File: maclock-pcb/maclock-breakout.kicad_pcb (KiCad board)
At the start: 2 copper layers, 70.5 x 26.5 mm, 19 parts, among them J1 BM02B-SRSS-TB(LF)(SN), J2 BM04B-SRSS-TB(LF)(SN), J3 B2B-PH-SM4-TB(LF)(SN), SW1 TSB001A3518A, SW2 TSB001A3518A, U1 PAM8302AASCR

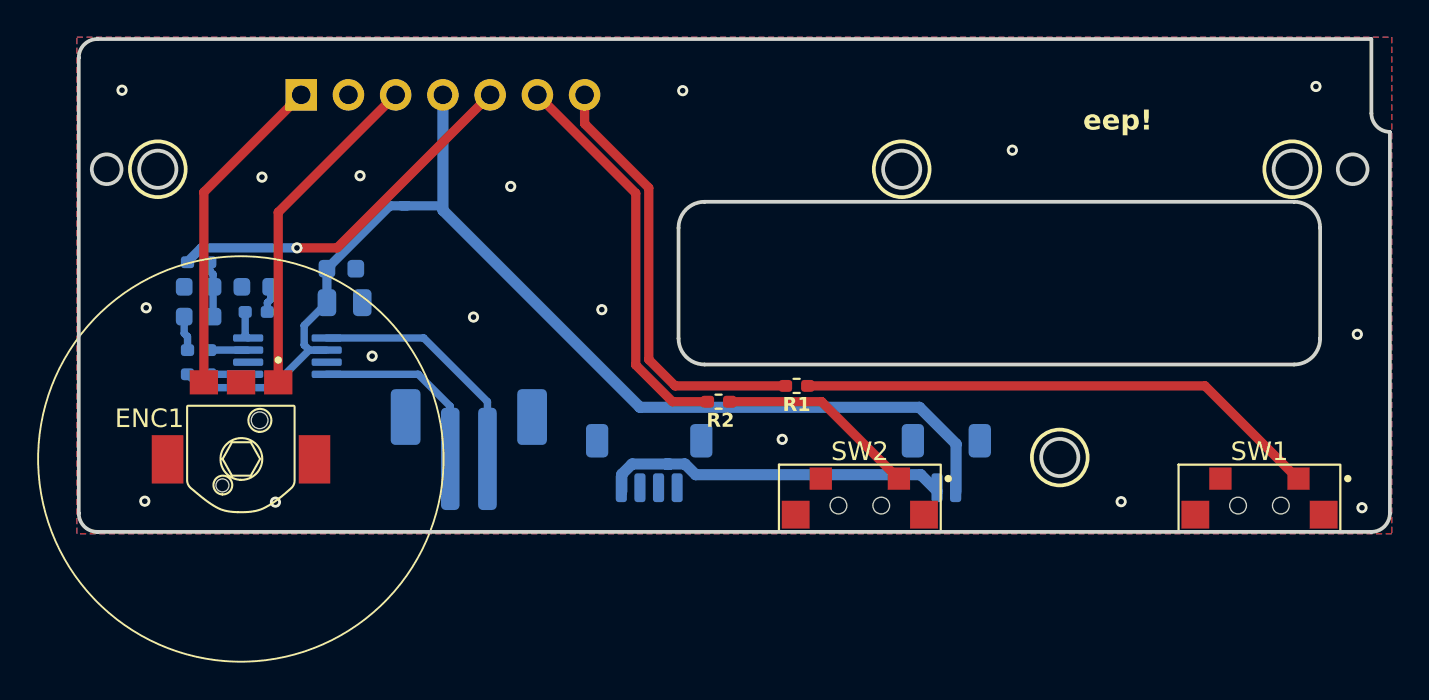
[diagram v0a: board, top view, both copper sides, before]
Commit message: PCB rev 2026.10: E8E8 dial, LCSC switches, PicoBlade connectors, clean schematic
Connectors: J1, J2 and J3 are Molex PicoBlade 1.25 mm (53398-0271 /
53398-0471), the pitch of the Maclock's own power, switch and speaker plugs;
the JST SH/PH parts on the first boards did not take them. The three now share
one row, 0.6 mm closer to the bottom edge, which also moves ENC1's rear post
hole out of J3's courtyard.

ENC1 is the F-Switch E8E8-3.2C60-9B34 (1.74 mm hex bore; the HYCW03's 1.78 mm
was too loose for the dial), sold by dicomon and not stocked at LCSC. Its
footprint is the proto board's Dial land with the origin on the bore, its
outline and 3D model (build123d STEP) are measured from a real part, and the
silkscreen shows the body and the 21 mm wheel's clearance. The symbol is KiCad's
encoder with an MP pin for the solder tabs. ENC_A/ENC_B are routed on F.Cu
straight to the pad centres.

SW1/SW2 use LCSC's own TSB001A3518A symbol, footprint and STEP (C2888448), in a
new `lcsc` project library imported with easyeda2kicad. Only the conversion
artefacts are fixed: NPTH peg holes, no outline stroke on the bracket pads (it
made them fail edge clearance), passive pins, one closed courtyard. The one-off
switch footprint and the HYCW03 footprint are gone; `maclock` now holds ENC1
only.

The schematic is rebuilt as one A4 sheet in functional blocks (Raspberry Pi,
power, buttons, dial, audio amplifier) with power symbols, notes and a filled
title block. Every part carries Manufacturer, MPN and LCSC fields, and ENC1 a
dicomon Supplier and link, so any exported BOM names the source. PiInput is J4.
Board nets and fields follow (GND, +5V, no-connect nets): schematic parity 0.

Also: C4/C5 ground pads get thermal reliefs (C1/C3 sit in pour too broken up to
form spokes and stay solid); the OSHW logo is removed, since the CC BY-NC-SA
licence is outside the OSHW definition; the board has a title block.
production/ (kicad-cli fab outputs) and the Fabrication Toolkit's options file
are 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
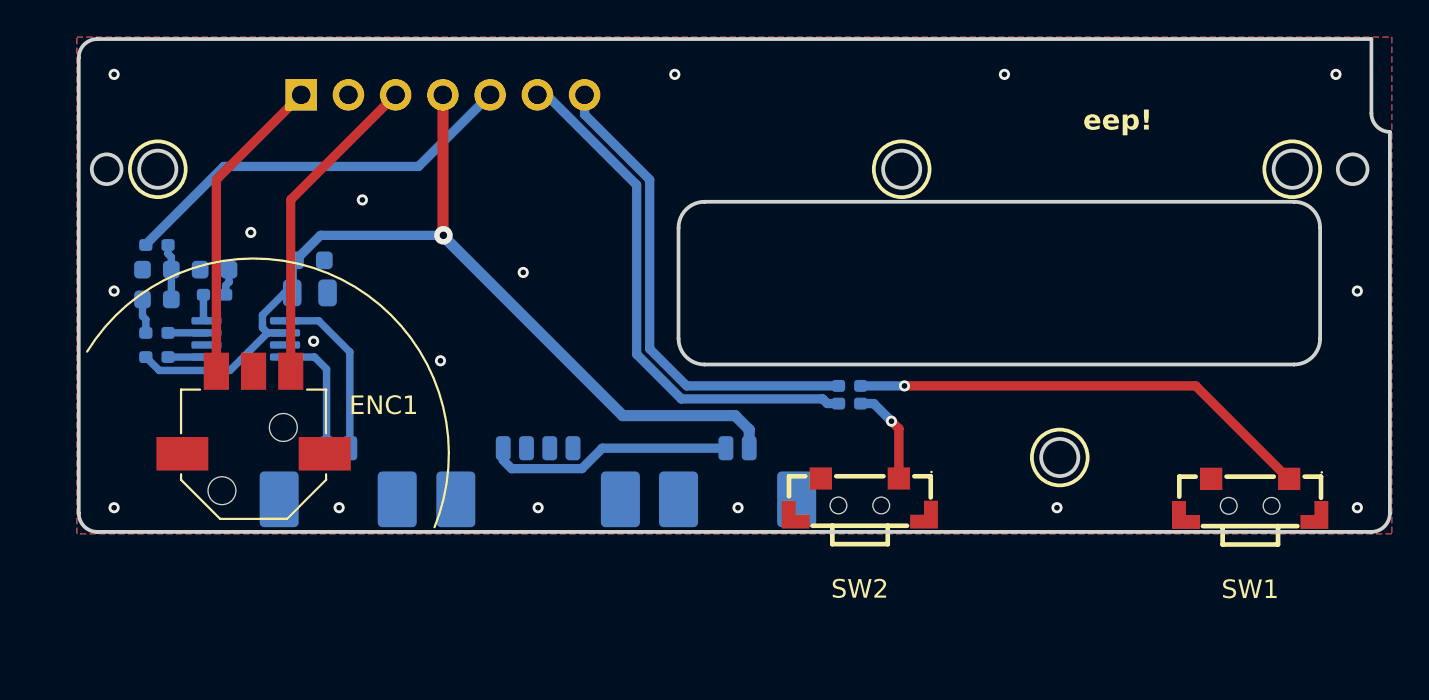
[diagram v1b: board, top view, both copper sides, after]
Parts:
- ENC1: value HYCW03-2.8D-5P-S -> E8E8-3.2C60-9B34; footprint maclock:RotaryEncoder_HYCW03-2.8D-5P-S_SMD -> maclock:RotaryEncoder_E8E8-3.2C60-9B34_SMD
- J1: value BM02B-SRSS-TB(LF)(SN) -> 53398-0271; footprint Connector_JST:JST_SH_BM02B-SRSS-TB_1x02-1MP_P1.00mm_Vertical -> Connector_Molex:Molex_PicoBlade_53398-0271_1x02-1MP_P1.25mm_Vertical
- J2: value BM04B-SRSS-TB(LF)(SN) -> 53398-0471; footprint Connector_JST:JST_SH_BM04B-SRSS-TB_1x04-1MP_P1.00mm_Vertical -> Connector_Molex:Molex_PicoBlade_53398-0471_1x04-1MP_P1.25mm_Vertical
- J3: value B2B-PH-SM4-TB(LF)(SN) -> 53398-0271; footprint Connector_JST:JST_PH_B2B-PH-SM4-TB_1x02-1MP_P2.00mm_Vertical -> Connector_Molex:Molex_PicoBlade_53398-0271_1x02-1MP_P1.25mm_Vertical
- J4: renamed from PiInput; value PZ254V-11-07P -> Pi GPIO
- R1, R2: value 1K -> 1k; moved to B.Cu
- R3: value 1K -> 1k
- R4, R5: value 47K -> 47k
- R6: value 100K -> 100k
- SW1, SW2: footprint maclock:SW_TSB001_7.7x3.55_SideSMD -> lcsc:SW-SMD_TSB001XXXX
- moved J1 11.2 mm to (152.9, 101.2)
- moved J3 7.12 mm to (131.4, 101.2)
- moved R2 7.05 mm to (158.9, 97.6)
- moved J2 5.99 mm to (142.2, 101.2)
- moved R1 2.85 mm to (158.9, 96.7)
- moved C3 2.43 mm to (124.8, 90.4)
- moved R5 2.43 mm to (124.8, 91.8)
- moved R6 2.43 mm to (121.7, 95.1)
- moved C1 2.43 mm to (121.7, 90.4)
- moved C2 2.43 mm to (121.7, 92.0)
- moved R3 2.43 mm to (121.7, 89.1)
- moved R4 2.43 mm to (121.7, 93.8)
- moved U1 2.43 mm to (126.5, 94.1)
- moved C5 1.94 mm to (129.9, 91.7)
- moved ENC1 1.89 mm to (126.9, 100.3), turned to 0 degrees
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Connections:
- net /5V renamed +5V
- C1 pad 1: /GND -> GND
- C3 pad 1: /GND -> GND
- C4 pad 2: /GND -> GND
- C5 pad 2: /GND -> GND
- ENC1 pad C: /GND -> GND
- J2 pad 1: (no net) -> unconnected-(J2-Pin_1-Pad1)
- J2 pad 2: (no net) -> unconnected-(J2-Pin_2-Pad2)
- J2 pad 3: /GND -> GND
- J4 pad 2: /GND -> GND
- SW1 pad 2: /GND -> GND
- SW1 pad 3: /GND -> GND
- SW1 pad 4: /GND -> GND
- SW2 pad 2: /GND -> GND
- SW2 pad 3: /GND -> GND
- SW2 pad 4: /GND -> GND
- U1 pad 2: (no net) -> unconnected-(U1-NC-Pad2)
- U1 pad 7: /GND -> GND
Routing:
- net +5V: track 63.1 -> 51.7 mm, vias 0 -> 1
- net /BTN2: track 21.4 -> 28.4 mm
- net /5V_IN: track 18.8 -> 13.3 mm
- net /SW2: track 10.8 -> 5.44 mm, vias 0 -> 1
- net /SPK+: track 13.1 -> 9.35 mm
- net /SPK-: track 10.2 -> 6.76 mm
- net /SW1: track 28.3 -> 25.2 mm, vias 0 -> 1
- net /BTN1: track 23.6 -> 26.1 mm
- net /AUDIO: track 20.0 -> 21.9 mm, vias 1 -> 0
- net /ENC_B: track 17.6 -> 16.7 mm
- net /ENC_A: track 18.1 -> 17.2 mm
- net GND: vias 0 -> 17
- net /GND: vias 17 -> 0
- added copper zone on B.Cu, net GND
- added copper zone on F.Cu, net GND
- removed copper zone on B.Cu, net /GND
- removed copper zone on F.Cu, net /GND
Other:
- board text added: "Wells Workshop https://wells.ee"
- board text added: "rev 2026.10"
- board text removed: "+"
- board text removed: "-"
- board text removed: "by Wells Workshop - https://wells.ee"
- board text removed: "rev 2026.09"

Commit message: Breakout: put back the Switch / Power / Speaker labels and J2's + / -
Rev 2026.10's field cleanup deleted the board-only "Label" field that
named J1-J3 on the back silk, leaving three identical PicoBlade sockets
and no polarity mark on the power input. The labels are back above the
connectors, now as a "Label" field on the schematic symbols too, so an
Update PCB from Schematic can't strip them again. "Speaker" sits 0.3 mm
right of centre to clear ENC1's peg hole. J2 gets + over pin 4 (5V) and
- over pin 3 (GND), as before.
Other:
- board text added: "+"
- board text added: "-"
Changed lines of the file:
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@@
 			)
 		)
+		(property "Label" "Speaker"
+			(at -0.3 4.2 0)
+			(layer "B.SilkS")
+			(effects
+				(font
+					(size 1.0795 1.0795)
+					(thickness 0.1905)
+				)
+				(justify mirror)
+			)
+		)
 		(attr smd)
 		(duplicate_pad_numbers_are_jumpers no)
@@
 			)
 		)
+		(property "Label" "Switch"
+			(at 0 4.2 0)
+			(layer "B.SilkS")
+			(effects
+				(font
+					(size 1.0795 1.0795)
+					(thickness 0.1905)
+				)
+				(justify mirror)
+			)
+		)
 		(attr smd)
 		(duplicate_pad_numbers_are_jumpers no)
@@
 			)
 		)
+		(property "Label" "Power"
+			(at 0 4.2 0)
+			(layer "B.SilkS")
+			(effects
+				(font
+					(size 1.0795 1.0795)
+					(thickness 0.1905)
+				)
+				(justify mirror)
+			)
+		)
 		(attr smd)
 		(duplicate_pad_numbers_are_jumpers no)
@@
 		)
 	)
+	(gr_text "+"
+		(at 140.325 98.5 0)
+		(layer "B.SilkS")
+		(effects
+			(font
+				(size 0.8 0.8)
+				(thickness 0.15)
+			)
+			(justify mirror)
+		)
+	)
+	(gr_text "-"
+		(at 141.575 98.5 0)
+		(layer "B.SilkS")
+		(effects
+			(font
+				(size 0.8 0.8)
+				(thickness 0.15)
+			)
+			(justify mirror)
+		)
+	)

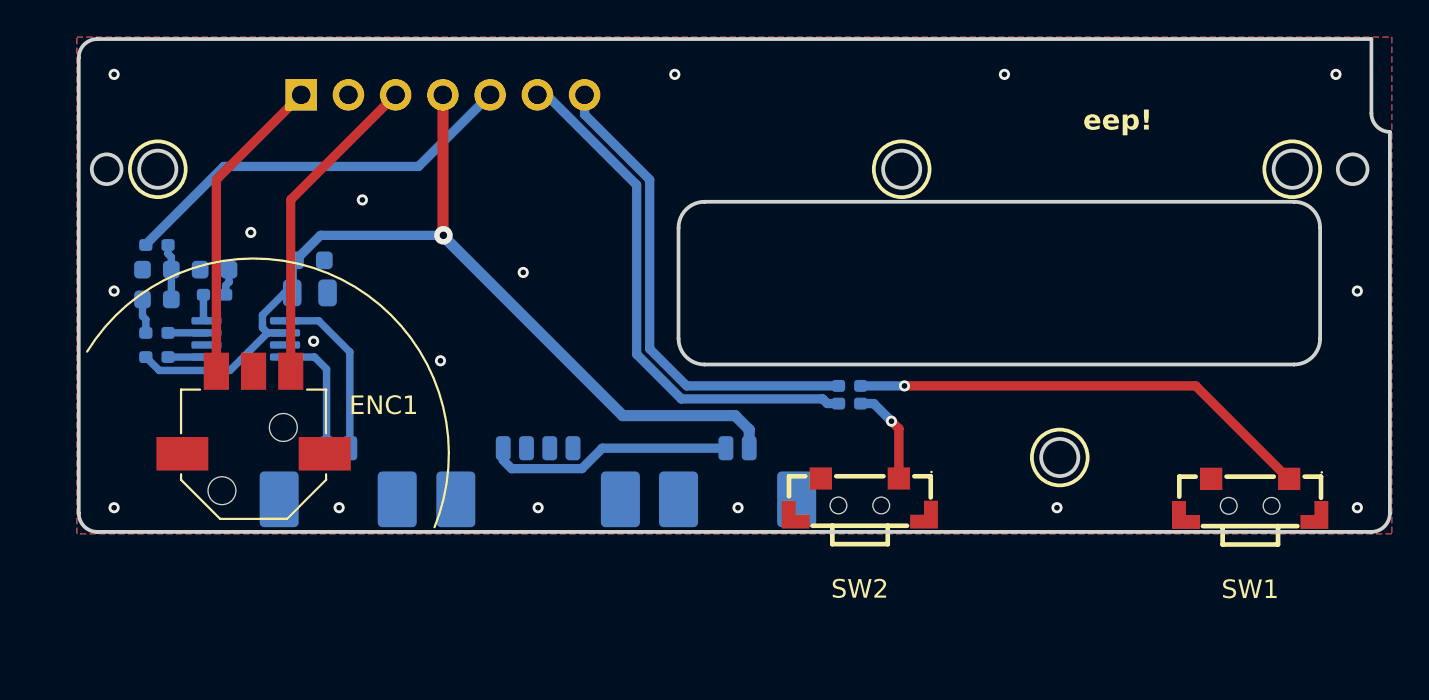
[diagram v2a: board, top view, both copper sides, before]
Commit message: PCB rev 2026.11: buffered audio input and a separate Pi ground return
Rev 2026.10 whines faintly with the Pi running. Recorded on the board and
traced, with the Pi powered both ways:

- The Pi's own supply current (Pi, display, backlight) ran through the
  amp's ground. Moving the Pi to USB power dropped the backlight's 1 kHz
  comb about 28 dB and removed the emulator's drifting tones. Holding
  GPIO 19 low or floating changed nothing on board power.
- On USB power, what was left rode on the audio pin itself: a 60 Hz-pulsed
  buzz from the Pi's 3.3 V (only while GPIO 19 runs PWM), and hiss from the
  Pi-to-board ground offset (gone when the pin floats).

Four new parts:

- J4 pin 2 is its own net, GND_PI, routed straight to J2 and joined to the
  board ground by net tie NT1 (copper only) at J2's ground pin. The amp's
  ground no longer carries the Pi's current.
- U2 (SN74LVC1G17) rebuilds GPIO 19 from U3 (TPS7A2033, low-noise 3.3 V),
  so only the timing of the Pi's signal reaches R3/C1 and the amp. C8 is
  U3's input cap; C10 sits between U3 and U2 as U3's output cap and U2's
  bypass. Both are the 1 uF part C4 already uses. R6 pulls SD up to the
  3.3 V rail, right beside U2.

Layout:

- U2, R3/C1 and R6 sit just left of U1, with U3, C8 and C10 tucked in
  beside U2, clear of the board edge.
- The amp and U3 take their 5 V from J1, at the start of the 5 V trunk, so
  the Pi's current on the trunk shares no copper with the amp's supply.
  That branch stays on the bottom layer and crosses under U1 between its
  pin rows rather than under the speaker leads, which leaves the top-layer
  ground plane unbroken under the amp. C4 stays against U1's VDD/GND
  pins; U1 turned so its outputs face J3.
- The audio line runs over the top of J4 on the bottom layer, so it never
  crosses GND_PI: no vias, header pinout unchanged.
- J1 (switch) and J2 (power) trade places, so NT1 and the 5 V tap sit at
  the ends of short, straight runs. Their silk labels move with them; J2's
  "+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
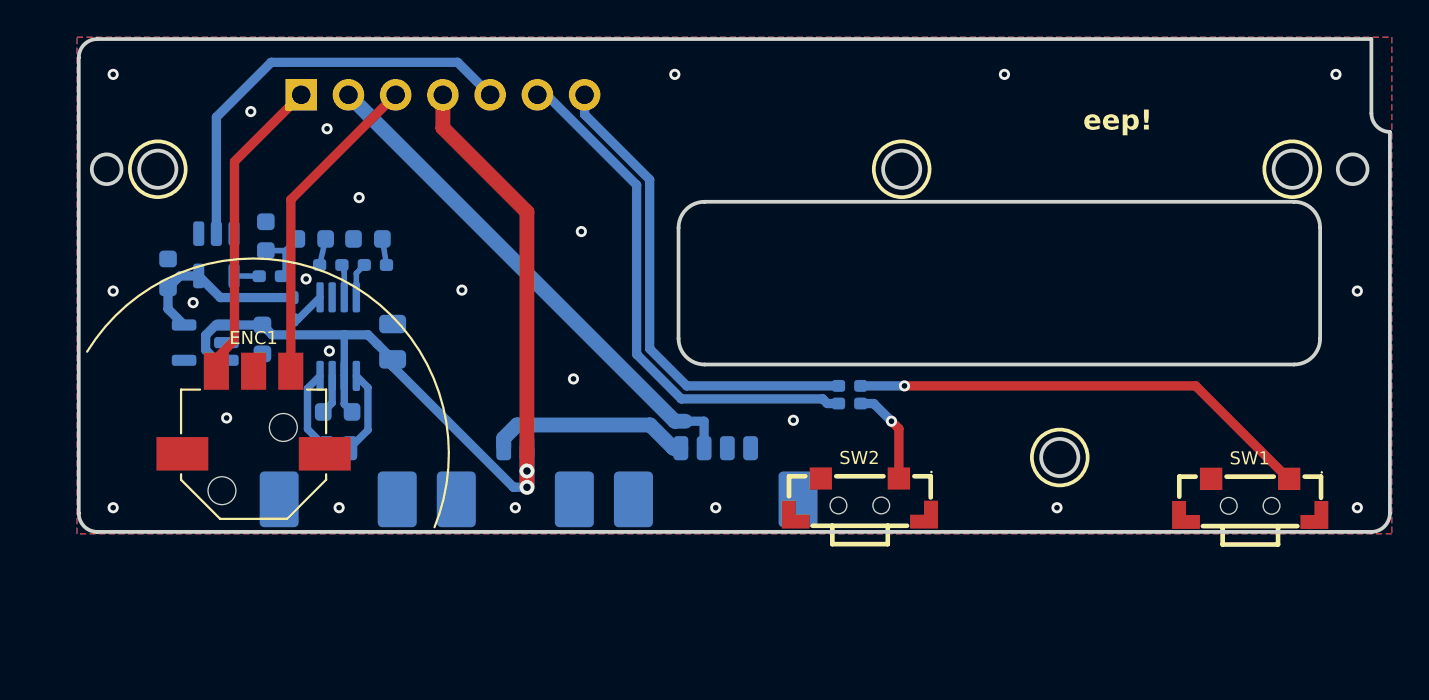
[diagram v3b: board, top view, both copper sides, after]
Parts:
- added C10: 1uF, Capacitor_SMD:C_0603_1608Metric, B.Cu at (122.3, 90.6)
- added C8: 1uF, Capacitor_SMD:C_0603_1608Metric, B.Cu at (127.4, 94.2)
- added NT1: NetTie_2, NetTie:NetTie-2_SMD_Pad0.5mm, B.Cu at (150.6, 98.5)
- added U2: SN74LVC1G17DBVR, Package_TO_SOT_SMD:SOT-23-5, B.Cu at (124.9, 89.6)
- added U3: TPS7A2033PDBVR, Package_TO_SOT_SMD:SOT-23-5, B.Cu at (124.3, 94.3)
- moved J1 12.0 mm to (141.0, 101.2)
- moved R4 10.0 mm to (131.1, 90.2)
- moved J2 9.55 mm to (151.8, 101.2)
- moved C2 8.91 mm to (130.0, 88.8), turned to 0 degrees
- moved R5 8.79 mm to (133.4, 90.2)
- moved C3 8.41 mm to (133.1, 88.8)
- moved C4 8.29 mm to (131.4, 98.0), turned to 180 degrees
- moved R6 7.75 mm to (129.0, 92.5), turned to -90 degrees
- moved R3 6.32 mm to (127.8, 90.8)
- moved C1 6.13 mm to (127.6, 88.6), turned to 90 degrees
- moved C5 5.16 mm to (134.4, 94.3), turned to 90 degrees
- moved U1 4.97 mm to (131.4, 94.0), turned to -90 degrees
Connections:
- C1 pad 1: GND -> /A+
- C1 pad 2: /A+ -> GND
- J4 pad 2: GND -> /GND_PI
- R3 pad 1: /AUDIO -> Net-(R3-Pad1)
- R6 pad 1: +5V -> +3V3
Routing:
- net /GND_PI: track 0.00 -> 25.4 mm
- net +3V3: track 0.00 -> 9.80 mm
- net /SPK+: track 9.35 -> 4.55 mm
- net GND: track 0.00 -> 3.59 mm, vias 17 -> 23
- net /5V_IN: track 13.3 -> 10.9 mm
- net /SPK-: track 6.76 -> 4.59 mm
- net Net-(R3-Pad1): track 0.00 -> 1.35 mm
- net +5V: track 51.7 -> 52.9 mm, vias 1 -> 2
- net /AUDIO: track 21.9 -> 22.9 mm
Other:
- board text added: "rev 2026.11"
- board text removed: "rev 2026.10"

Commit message: Battery supply is about 4 V: document the burble, drop U3 to 3.0 V
The Maclock's charging board doesn't boost the 18650 to 5 V. Its output is
the cell: about 4.15 V with no load and 4.00 V with the Pi running, and the
same with the charge cable plugged in. vcgencmd get_throttled still read 0x0
at 4.00 V, so the Pi doesn't catch it.

On a rev 2026.10 board this puts a constant burble in the speaker, louder
as the brightness goes up. A phone recording with GPIO 19 switched from PWM
to a static low (emulator still running) shows the 3-4.25 kHz and
5.5-6 kHz noise falling about 10 dB to the floor and returning with PWM. So
it rides on the audio pin's high level, the Pi's 3.3 V made from ~4 V, and
the amp's own supply and ground are clean. That is the path rev 2026.11's
U2/U3 rebuild takes out.

U3 TPS7A2033 -> TPS7A2030 (LCSC C963429, same SOT-23-5, no layout change),
net +3V3 renamed +3V0. A 3.3 V LDO has about 0.7 V of headroom at full
charge and runs into dropout as the cell drains, where it stops filtering;
3.0 V keeps it regulating over the battery's range. The audio drive drops
0.8 dB, which offsets some of the amp's lost headroom at 4 V. TPS7A20 takes
1.6-6.0 V in, so a real 5 V supply is fine too. ERC 0; DRC unchanged (0
unconnected, 0 parity); netlist identical apart from the rename.

Docs: a Known Issues entry and a troubleshooting line for the burble, and
every claim that the board or Pi runs on 5 V now says about 4 V. Pin and
net names (5V, +5V) stay as labels. The interposer drawing's aria-label
still says "5 V"; it's exported from the shop, so that fix belongs there.
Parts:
- U3: value TPS7A2033PDBVR -> TPS7A2030PDBVR
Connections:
- net +3V3 renamed +3V0
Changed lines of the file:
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@@
 			(layers "B.Cu" "B.Mask" "B.Paste")
 			(roundrect_rratio 0.25)
-			(net "+3V3")
+			(net "+3V0")
 		)
 		(embedded_fonts no)
@@
 			(layers "B.Cu" "B.Mask" "B.Paste")
 			(roundrect_rratio 0.25)
-			(net "+3V3")
+			(net "+3V0")
 		)
 		(pad "2" smd roundrect
@@
 			(layers "B.Cu" "B.Mask" "B.Paste")
 			(roundrect_rratio 0.25)
-			(net "+3V3")
+			(net "+3V0")
 		)
 		(pad "2" smd roundrect
@@
 			)
 		)
-		(property "Value" "TPS7A2033PDBVR"
+		(property "Value" "TPS7A2030PDBVR"
 			(at 0 -2.4 0)
 			(layer "B.Fab")
@@
 			)
 		)
-		(property "Description" "300 mA low-noise LDO, 3.3 V, SOT-23-5"
+		(property "Description" "300 mA low-noise LDO, 3.0 V, SOT-23-5"
 			(at 0 0 0)
 			(layer "B.Fab")
@@
 			)
 		)
-		(property "MPN" "TPS7A2033PDBVR"
+		(property "MPN" "TPS7A2030PDBVR"
 			(at 0 0 0)
 			(layer "B.Fab")
@@
 			)
 		)
-		(property "LCSC" "C2862740"
+		(property "LCSC" "C963429"
 			(at 0 0 0)
 			(layer "B.Fab")
@@
 			(layers "B.Cu" "B.Mask" "B.Paste")
 			(roundrect_rratio 0.25)
-			(net "+3V3")
+			(net "+3V0")
 		)
 		(embedded_fonts no)
@@
 		(width 0.5)
 		(layer "B.Cu")
-		(net "+3V3")
+		(net "+3V0")
 	)
 	(segment
@@
 		(width 0.5)
 		(layer "B.Cu")
-		(net "+3V3")
+		(net "+3V0")
 	)
 	(segment
@@
 		(width 0.5)
 		(layer "B.Cu")
-		(net "+3V3")
+		(net "+3V0")
 	)
 	(segment
@@
 		(width 0.5)
 		(layer "B.Cu")
-		(net "+3V3")
+		(net "+3V0")
 	)
 	(segment
@@
 		(width 0.5)
 		(layer "B.Cu")
-		(net "+3V3")
+		(net "+3V0")
 	)
 	(segment
@@
 		(width 0.5)
 		(layer "B.Cu")
-		(net "+3V3")
+		(net "+3V0")
 	)
 	(segment
